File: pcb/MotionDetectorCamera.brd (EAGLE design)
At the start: 100 x 80 mm, 80 parts, among them U1 AT25XV041B-SSHV-T_AT25XV041B-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, U2 TPS62801X_TPS6280X, U3 TPS62801X_TPS6280X, U4 TPS6380X_TPS6380X, U5 LATTICE-SEMICONDUCTOR---ICE40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, U6 MICRON---MT48H32M16LFB4-6-IT: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, X1 CON-COAX_734120110, X10 CON-COAX_734120110, X2 CON-COAX_734120110, X3 CON-COAX_734120110, X4 CON-COAX_734120110, X5 CON-COAX_734120110, X6 CON-COAX_734120110, X7 CON-COAX_734120110, X8 CON-COAX_734120110, X9 CON-COAX_734120110, Y1 SIT8021AI-J4-XXS-12.000000E_S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

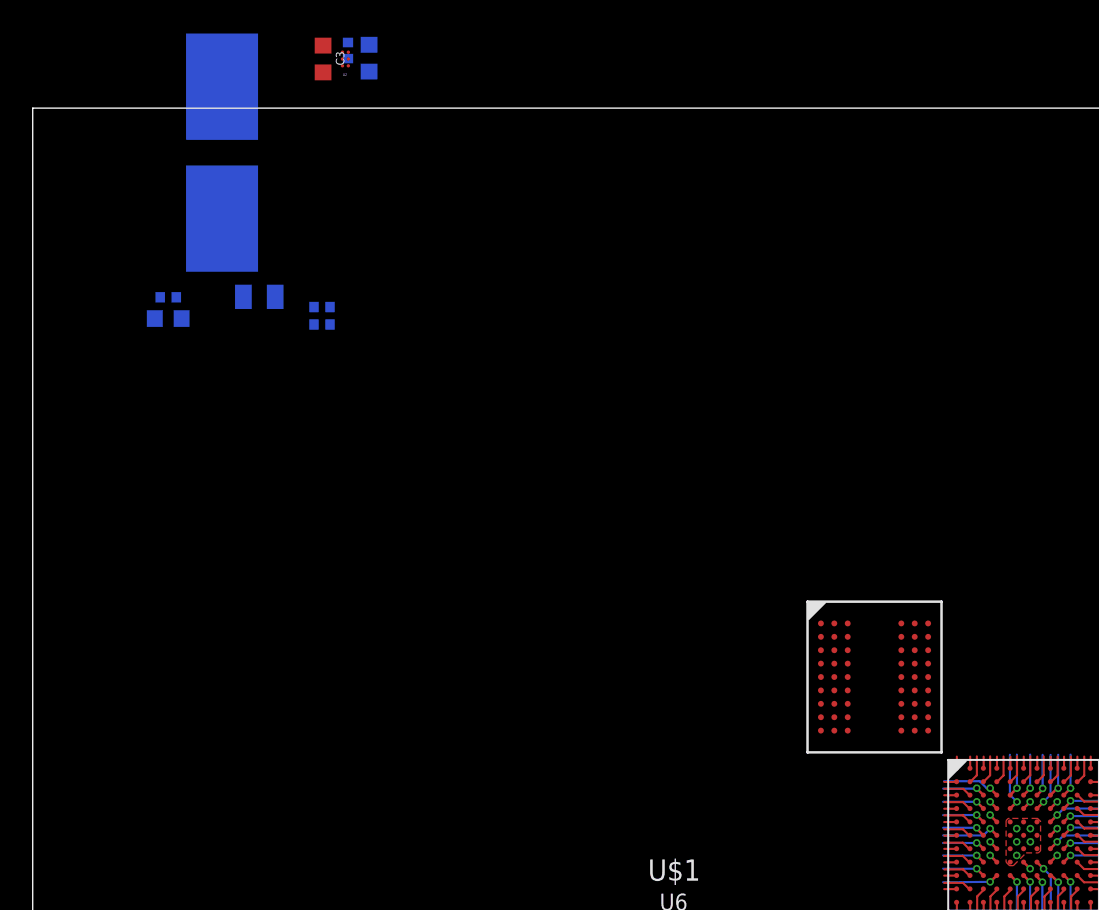
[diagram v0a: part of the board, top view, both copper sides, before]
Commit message: Laid power pours
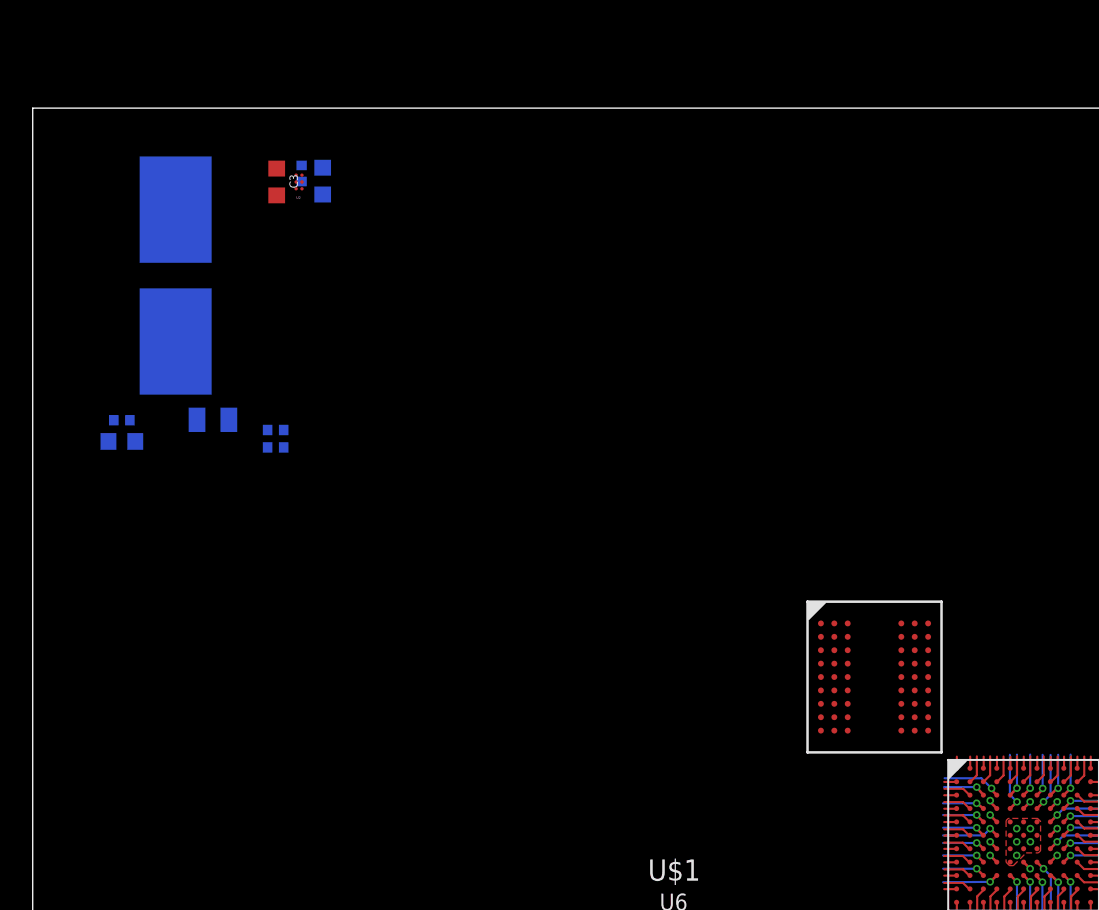
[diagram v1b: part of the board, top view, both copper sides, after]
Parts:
- moved C2 7.85 mm to (17.3, 75.6)
- moved C21 7.85 mm to (14.5, 59.7)
- moved R3 7.85 mm to (16.1, 76.1)
- moved C12 7.85 mm to (5.32, 60.1)
- moved C13 7.85 mm to (5.32, 61.4)
- moved C20 7.85 mm to (14.5, 60.8)
- moved C3 7.85 mm to (14.6, 75.6)
- moved L1 7.85 mm to (8.53, 69.7)
- moved R20 7.85 mm to (10.8, 61.4)
- moved U2 7.85 mm to (15.9, 75.6)
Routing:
- added copper zone on layer 15, net 1V2

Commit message: Moved 1V8 connection to bottom of ice40 so our power supply won't be in the way of our routing
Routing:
- net 1V2: track 2.33 -> 49.2 mm
- net 1V8: track 7.19 -> 29.4 mm
- removed copper zone on layer 15, net 1V2
- removed copper zone on layer 15, net 1V8
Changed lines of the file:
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@@
 <wire x1="59.5503" y1="34.5927" x2="59.5503" y2="34.58971875" width="0.1524" layer="1"/>
 <wire x1="63.17" y1="31.822" x2="63.17" y2="32.482" width="0.127" layer="1"/>
-<polygon width="0.1524" layer="15" rank="0">
-<vertex x="56.769" y="36.6014"/>
-<vertex x="56.769" y="35.9664"/>
-<vertex x="56.9722" y="35.7632"/>
-<vertex x="57.6072" y="35.7632"/>
-<vertex x="59.1566" y="34.2138"/>
-<vertex x="59.9694" y="34.2138"/>
-<vertex x="59.9694" y="35.0266"/>
-<vertex x="59.944" y="35.052"/>
-<vertex x="60.706" y="35.814"/>
-<vertex x="60.706" y="36.576"/>
-<vertex x="60.8076" y="36.6776"/>
-<vertex x="61.5188" y="36.6776"/>
-<vertex x="61.5188" y="37.2872"/>
-<vertex x="61.468" y="37.338"/>
-<vertex x="60.7568" y="37.338"/>
-<vertex x="59.2328" y="38.862"/>
-<vertex x="59.2328" y="41.0718"/>
-<vertex x="57.7088" y="41.0718"/>
-<vertex x="57.7088" y="38.5318"/>
-<vertex x="57.3786" y="38.2016"/>
-<vertex x="56.8198" y="38.2016"/>
-<vertex x="56.8198" y="37.5158"/>
-<vertex x="56.7944" y="37.4904"/>
-<vertex x="57.6072" y="37.4904"/>
-<vertex x="57.6326" y="37.465"/>
-<vertex x="57.6326" y="36.6522"/>
-<vertex x="57.5818" y="36.6014"/>
-</polygon>
+<wire x1="56.769" y1="36.6014" x2="56.769" y2="35.9664" width="0.1524" layer="15"/>
+<wire x1="56.769" y1="35.9664" x2="56.9722" y2="35.7632" width="0.1524" layer="15"/>
+<wire x1="56.9722" y1="35.7632" x2="57.6072" y2="35.7632" width="0.1524" layer="15"/>
+<wire x1="57.6072" y1="35.7632" x2="59.1566" y2="34.2138" width="0.1524" layer="15"/>
+<wire x1="59.1566" y1="34.2138" x2="59.9694" y2="34.2138" width="0.1524" layer="15"/>
+<wire x1="59.9694" y1="34.2138" x2="59.9694" y2="35.0266" width="0.1524" layer="15"/>
+<wire x1="59.9694" y1="35.0266" x2="59.944" y2="35.052" width="0.1524" layer="15"/>
+<wire x1="59.944" y1="35.052" x2="60.706" y2="35.814" width="0.1524" layer="15"/>
+<wire x1="60.706" y1="35.814" x2="60.706" y2="36.576" width="0.1524" layer="15"/>
+<wire x1="60.706" y1="36.576" x2="60.8076" y2="36.6776" width="0.1524" layer="15"/>
+<wire x1="60.8076" y1="36.6776" x2="61.5188" y2="36.6776" width="0.1524" layer="15"/>
+<wire x1="61.5188" y1="36.6776" x2="61.5188" y2="37.2872" width="0.1524" layer="15"/>
+<wire x1="61.5188" y1="37.2872" x2="61.468" y2="37.338" width="0.1524" layer="15"/>
+<wire x1="61.468" y1="37.338" x2="60.7568" y2="37.338" width="0.1524" layer="15"/>
+<wire x1="60.7568" y1="37.338" x2="59.2328" y2="38.862" width="0.1524" layer="15"/>
+<wire x1="59.2328" y1="38.862" x2="59.2328" y2="41.0718" width="0.1524" layer="15"/>
+<wire x1="59.2328" y1="41.0718" x2="57.7088" y2="41.0718" width="0.1524" layer="15"/>
+<wire x1="57.7088" y1="41.0718" x2="57.7088" y2="38.5318" width="0.1524" layer="15"/>
+<wire x1="57.7088" y1="38.5318" x2="57.3786" y2="38.2016" width="0.1524" layer="15"/>
+<wire x1="57.3786" y1="38.2016" x2="56.8198" y2="38.2016" width="0.1524" layer="15"/>
+<wire x1="56.8198" y1="38.2016" x2="56.8198" y2="37.5158" width="0.1524" layer="15"/>
+<wire x1="56.8198" y1="37.5158" x2="56.7944" y2="37.4904" width="0.1524" layer="15"/>
+<wire x1="56.7944" y1="37.4904" x2="57.6072" y2="37.4904" width="0.1524" layer="15"/>
+<wire x1="57.6072" y1="37.4904" x2="57.6326" y2="37.465" width="0.1524" layer="15"/>
+<wire x1="57.6326" y1="37.465" x2="57.6326" y2="36.6522" width="0.1524" layer="15"/>
+<wire x1="57.6326" y1="36.6522" x2="57.5818" y2="36.6014" width="0.1524" layer="15"/>
+<wire x1="57.5818" y1="36.6014" x2="56.769" y2="36.6014" width="0.1524" layer="15"/>
 <wire x1="51.859" y1="49.234" x2="53.459" y2="49.234" width="0" layer="19" extent="1-1"/>
 <wire x1="51.859" y1="47.634" x2="51.859" y2="49.234" width="0" layer="19" extent="1-1"/>
@@
 <wire x1="53.459" y1="42.834" x2="51.859" y2="46.034" width="0" layer="19" extent="1-1"/>
 <wire x1="57.1627" y1="37.7952" x2="53.459" y2="42.834" width="0" layer="19" extent="1-1"/>
+<wire x1="57.1627" y1="36.195" x2="57.559" y2="37.384" width="0" layer="19" extent="1-1"/>
+<wire x1="59.159" y1="38.184" x2="57.559" y2="37.384" width="0" layer="19" extent="1-1"/>
+<wire x1="59.159" y1="34.984" x2="57.559" y2="35.784" width="0" layer="19" extent="1-1"/>
+<wire x1="61.1632" y1="36.9824" x2="59.5503" y2="38.5826" width="0" layer="19" extent="1-1"/>
 <wire x1="63.159" y1="32.584" x2="59.5503" y2="34.58971875" width="0" layer="19" extent="1-1"/>
 <wire x1="63.17" y1="32.482" x2="63.159" y2="32.584" width="0" layer="19" extent="1-1"/>
@@
 <wire x1="60.759" y1="34.984" x2="61.1572" y2="35.3822" width="0.1524" layer="1"/>
 <wire x1="61.1572" y1="35.3822" x2="61.1632" y2="35.3822" width="0.1524" layer="1"/>
-<polygon width="0.1524" layer="15" rank="2">
-<vertex x="63.7794" y="31.8262"/>
-<vertex x="54.6354" y="31.8262"/>
-<vertex x="54.6354" y="41.0972"/>
-<vertex x="57.5056" y="41.0972"/>
-<vertex x="57.5056" y="35.8394"/>
-<vertex x="59.436" y="35.8394"/>
-<vertex x="59.436" y="41.0972"/>
-<vertex x="63.7794" y="41.0972"/>
-</polygon>
-<wire x1="57.165240625" y1="38.653721875" x2="11.7094" y2="61.3918" width="0" layer="19" extent="16-16"/>
+<wire x1="54.6354" y1="41.0972" x2="54.6354" y2="32.0802" width="0.1524" layer="15"/>
+<wire x1="54.6354" y1="32.0802" x2="63.8302" y2="32.0802" width="0.1524" layer="15"/>
+<wire x1="63.8302" y1="32.0802" x2="63.8302" y2="41.0718" width="0.1524" layer="15"/>
+<wire x1="63.8302" y1="41.0718" x2="59.436" y2="41.0718" width="0.1524" layer="15"/>
+<wire x1="59.436" y1="41.0718" x2="59.436" y2="35.8394" width="0.1524" layer="15"/>
+<wire x1="59.436" y1="35.8394" x2="57.5056" y2="35.8394" width="0.1524" layer="15"/>
+<wire x1="57.5056" y1="35.8394" x2="57.5056" y2="41.0972" width="0.1524" layer="15"/>
+<wire x1="57.5056" y1="41.0972" x2="54.6354" y2="41.0972" width="0.1524" layer="15"/>
+<wire x1="61.1632" y1="35.3822" x2="60.759" y2="38.184" width="0" layer="19" extent="1-1"/>
+<wire x1="57.559" y1="38.184" x2="60.759" y2="38.184" width="0" layer="19" extent="1-1"/>
+<wire x1="57.1627" y1="35.3822" x2="57.559" y2="38.184" width="0" layer="19" extent="1-1"/>
+<wire x1="11.7094" y1="61.3918" x2="57.165240625" y2="38.653721875" width="0" layer="19" extent="16-16"/>
 <wire x1="33.5534" y1="-25.174" x2="57.559" y2="34.984" width="0" layer="19" extent="1-16"/>
 <wire x1="32.512" y1="-25.174" x2="33.5534" y2="-25.174" width="0" layer="19" extent="16-16"/>

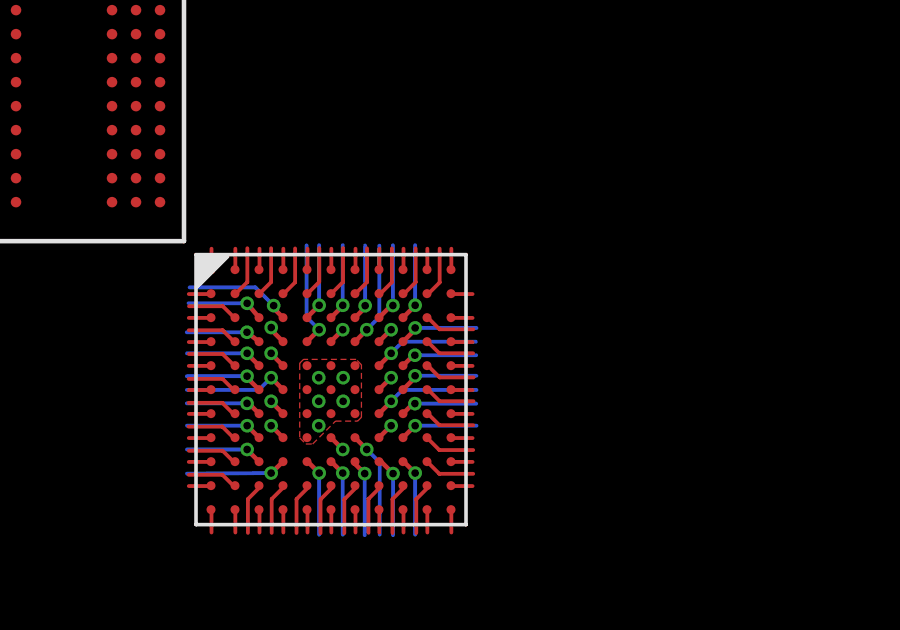
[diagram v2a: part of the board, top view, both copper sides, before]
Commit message: Routed 2V5 pour
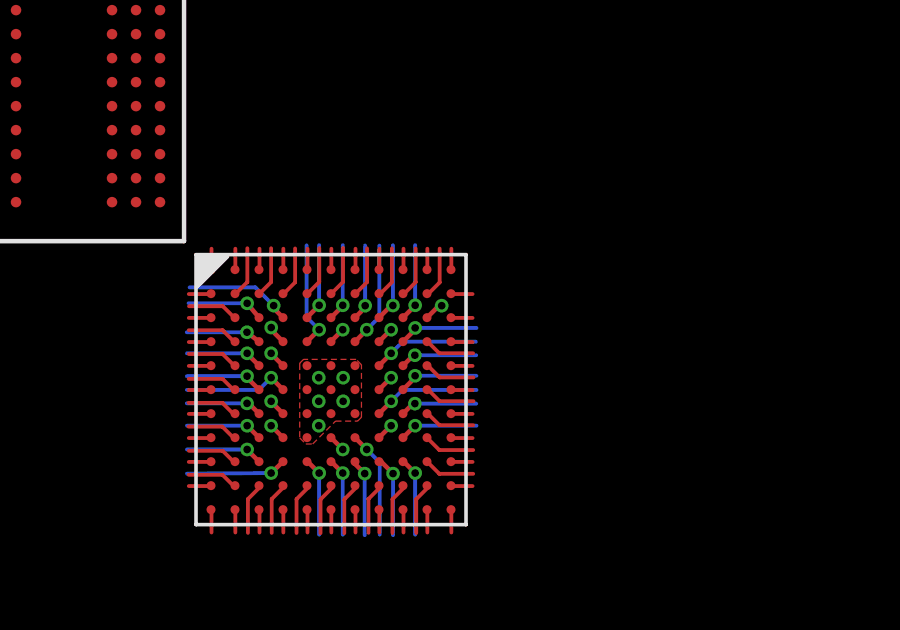
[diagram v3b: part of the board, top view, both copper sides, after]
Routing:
- net 1V2: track 49.2 -> 2.36 mm
- net 1V8: track 29.4 -> 7.19 mm
- net 2V5: track 1.65 -> 0.65 mm, vias 0 -> 1
- added copper zone on layer 15, net 1V2
- added copper zone on layer 15, net 1V8
- added copper zone on layer 15, net 2V5
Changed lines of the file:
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@@
 <wire x1="59.5503" y1="34.5927" x2="59.5503" y2="34.58971875" width="0.1524" layer="1"/>
 <wire x1="63.17" y1="31.822" x2="63.17" y2="32.482" width="0.127" layer="1"/>
-<wire x1="56.769" y1="36.6014" x2="56.769" y2="35.9664" width="0.1524" layer="15"/>
-<wire x1="56.769" y1="35.9664" x2="56.9722" y2="35.7632" width="0.1524" layer="15"/>
-<wire x1="56.9722" y1="35.7632" x2="57.6072" y2="35.7632" width="0.1524" layer="15"/>
-<wire x1="57.6072" y1="35.7632" x2="59.1566" y2="34.2138" width="0.1524" layer="15"/>
-<wire x1="59.1566" y1="34.2138" x2="59.9694" y2="34.2138" width="0.1524" layer="15"/>
-<wire x1="59.9694" y1="34.2138" x2="59.9694" y2="35.0266" width="0.1524" layer="15"/>
-<wire x1="59.9694" y1="35.0266" x2="59.944" y2="35.052" width="0.1524" layer="15"/>
-<wire x1="59.944" y1="35.052" x2="60.706" y2="35.814" width="0.1524" layer="15"/>
-<wire x1="60.706" y1="35.814" x2="60.706" y2="36.576" width="0.1524" layer="15"/>
-<wire x1="60.706" y1="36.576" x2="60.8076" y2="36.6776" width="0.1524" layer="15"/>
-<wire x1="60.8076" y1="36.6776" x2="61.5188" y2="36.6776" width="0.1524" layer="15"/>
-<wire x1="61.5188" y1="36.6776" x2="61.5188" y2="37.2872" width="0.1524" layer="15"/>
-<wire x1="61.5188" y1="37.2872" x2="61.468" y2="37.338" width="0.1524" layer="15"/>
-<wire x1="61.468" y1="37.338" x2="60.7568" y2="37.338" width="0.1524" layer="15"/>
-<wire x1="60.7568" y1="37.338" x2="59.2328" y2="38.862" width="0.1524" layer="15"/>
-<wire x1="59.2328" y1="38.862" x2="59.2328" y2="41.0718" width="0.1524" layer="15"/>
-<wire x1="59.2328" y1="41.0718" x2="57.7088" y2="41.0718" width="0.1524" layer="15"/>
-<wire x1="57.7088" y1="41.0718" x2="57.7088" y2="38.5318" width="0.1524" layer="15"/>
-<wire x1="57.7088" y1="38.5318" x2="57.3786" y2="38.2016" width="0.1524" layer="15"/>
-<wire x1="57.3786" y1="38.2016" x2="56.8198" y2="38.2016" width="0.1524" layer="15"/>
-<wire x1="56.8198" y1="38.2016" x2="56.8198" y2="37.5158" width="0.1524" layer="15"/>
-<wire x1="56.8198" y1="37.5158" x2="56.7944" y2="37.4904" width="0.1524" layer="15"/>
-<wire x1="56.7944" y1="37.4904" x2="57.6072" y2="37.4904" width="0.1524" layer="15"/>
-<wire x1="57.6072" y1="37.4904" x2="57.6326" y2="37.465" width="0.1524" layer="15"/>
-<wire x1="57.6326" y1="37.465" x2="57.6326" y2="36.6522" width="0.1524" layer="15"/>
-<wire x1="57.6326" y1="36.6522" x2="57.5818" y2="36.6014" width="0.1524" layer="15"/>
-<wire x1="57.5818" y1="36.6014" x2="56.769" y2="36.6014" width="0.1524" layer="15"/>
+<polygon width="0.1524" layer="15" rank="0">
+<vertex x="56.769" y="36.6014"/>
+<vertex x="56.769" y="35.9664"/>
+<vertex x="56.9722" y="35.7632"/>
+<vertex x="57.6326" y="35.7632"/>
+<vertex x="57.6326" y="31.75"/>
+<vertex x="59.9694" y="31.75"/>
+<vertex x="59.9694" y="35.0266"/>
+<vertex x="59.944" y="35.052"/>
+<vertex x="60.706" y="35.814"/>
+<vertex x="60.706" y="36.576"/>
+<vertex x="60.8076" y="36.6776"/>
+<vertex x="61.5188" y="36.6776"/>
+<vertex x="61.5188" y="37.2872"/>
+<vertex x="61.468" y="37.338"/>
+<vertex x="60.7568" y="37.338"/>
+<vertex x="59.2328" y="38.862"/>
+<vertex x="59.2328" y="39.3954"/>
+<vertex x="57.7088" y="39.3954"/>
+<vertex x="57.7088" y="38.5318"/>
+<vertex x="57.3786" y="38.2016"/>
+<vertex x="56.8198" y="38.2016"/>
+<vertex x="56.8198" y="37.5158"/>
+<vertex x="56.7944" y="37.4904"/>
+<vertex x="57.6072" y="37.4904"/>
+<vertex x="57.6326" y="37.465"/>
+<vertex x="57.6326" y="36.6522"/>
+<vertex x="57.5818" y="36.6014"/>
+</polygon>
 <wire x1="51.859" y1="49.234" x2="53.459" y2="49.234" width="0" layer="19" extent="1-1"/>
 <wire x1="51.859" y1="47.634" x2="51.859" y2="49.234" width="0" layer="19" extent="1-1"/>
@@
 <wire x1="53.459" y1="42.834" x2="51.859" y2="46.034" width="0" layer="19" extent="1-1"/>
 <wire x1="57.1627" y1="37.7952" x2="53.459" y2="42.834" width="0" layer="19" extent="1-1"/>
-<wire x1="57.1627" y1="36.195" x2="57.559" y2="37.384" width="0" layer="19" extent="1-1"/>
-<wire x1="59.159" y1="38.184" x2="57.559" y2="37.384" width="0" layer="19" extent="1-1"/>
-<wire x1="59.159" y1="34.984" x2="57.559" y2="35.784" width="0" layer="19" extent="1-1"/>
-<wire x1="61.1632" y1="36.9824" x2="59.5503" y2="38.5826" width="0" layer="19" extent="1-1"/>
 <wire x1="63.159" y1="32.584" x2="59.5503" y2="34.58971875" width="0" layer="19" extent="1-1"/>
 <wire x1="63.17" y1="32.482" x2="63.159" y2="32.584" width="0" layer="19" extent="1-1"/>
@@
 <wire x1="60.759" y1="34.984" x2="61.1572" y2="35.3822" width="0.1524" layer="1"/>
 <wire x1="61.1572" y1="35.3822" x2="61.1632" y2="35.3822" width="0.1524" layer="1"/>
-<wire x1="54.6354" y1="41.0972" x2="54.6354" y2="32.0802" width="0.1524" layer="15"/>
-<wire x1="54.6354" y1="32.0802" x2="63.8302" y2="32.0802" width="0.1524" layer="15"/>
-<wire x1="63.8302" y1="32.0802" x2="63.8302" y2="41.0718" width="0.1524" layer="15"/>
-<wire x1="63.8302" y1="41.0718" x2="59.436" y2="41.0718" width="0.1524" layer="15"/>
-<wire x1="59.436" y1="41.0718" x2="59.436" y2="35.8394" width="0.1524" layer="15"/>
-<wire x1="59.436" y1="35.8394" x2="57.5056" y2="35.8394" width="0.1524" layer="15"/>
-<wire x1="57.5056" y1="35.8394" x2="57.5056" y2="41.0972" width="0.1524" layer="15"/>
-<wire x1="57.5056" y1="41.0972" x2="54.6354" y2="41.0972" width="0.1524" layer="15"/>
-<wire x1="61.1632" y1="35.3822" x2="60.759" y2="38.184" width="0" layer="19" extent="1-1"/>
-<wire x1="57.559" y1="38.184" x2="60.759" y2="38.184" width="0" layer="19" extent="1-1"/>
-<wire x1="57.1627" y1="35.3822" x2="57.559" y2="38.184" width="0" layer="19" extent="1-1"/>
-<wire x1="11.7094" y1="61.3918" x2="57.165240625" y2="38.653721875" width="0" layer="19" extent="16-16"/>
+<wire x1="57.5056" y1="41.0718" x2="57.5056" y2="41.0972" width="0.1524" layer="15"/>
+<polygon width="0.1524" layer="15" rank="3">
+<vertex x="63.8302" y="32.0802"/>
+<vertex x="54.6354" y="32.0802"/>
+<vertex x="54.6354" y="41.0972"/>
+<vertex x="63.8302" y="41.0972"/>
+</polygon>
+<wire x1="57.5056" y1="41.0972" x2="11.7094" y2="61.3918" width="0" layer="19" extent="15-16"/>
 <wire x1="33.5534" y1="-25.174" x2="57.559" y2="34.984" width="0" layer="19" extent="1-16"/>
 <wire x1="32.512" y1="-25.174" x2="33.5534" y2="-25.174" width="0" layer="19" extent="16-16"/>
@@
 <contactref element="C29" pad="1"/>
 <contactref element="U$1" pad="C10"/>
-<wire x1="62.406" y1="38.96551875" x2="62.77551875" y2="38.596" width="0.127" layer="1"/>
-<wire x1="62.77551875" y1="38.596" x2="63.903459375" y2="38.596" width="0.127" layer="1"/>
-<wire x1="62.406" y1="38.96551875" x2="62.359" y2="38.984" width="0" layer="19" extent="1-1"/>
-<wire x1="64.775" y1="-18.415" x2="63.903459375" y2="38.596" width="0" layer="19" extent="1-16"/>
+<wire x1="62.359" y1="38.984" x2="62.7577125" y2="39.3827125" width="0.1524" layer="1"/>
+<wire x1="62.7577125" y1="39.3827125" x2="62.847253125" y2="39.3827" width="0.1524" layer="1"/>
+<via x="62.847253125" y="39.3827" extent="1-16" drill="0.254"/>
+<polygon width="0.1524" layer="15" rank="2">
+<vertex x="62.6872" y="39.6494"/>
+<vertex x="62.6872" y="39.116"/>
+<vertex x="64.897" y="39.116"/>
+<vertex x="64.897" y="39.6494"/>
+</polygon>
 <wire x1="35.334" y1="-54.356" x2="64.775" y2="-18.415" width="0" layer="19" extent="1-16"/>
 <wire x1="35.334" y1="-56.134" x2="35.334" y2="-54.356" width="0" layer="19" extent="1-1"/>
+<wire x1="62.359" y1="38.984" x2="64.775" y2="-18.415" width="0" layer="19" extent="1-16"/>
 </signal>
 <signal name="N$12">
